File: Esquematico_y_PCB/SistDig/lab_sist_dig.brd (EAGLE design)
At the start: 93.8 x 85.2 mm, 25 parts

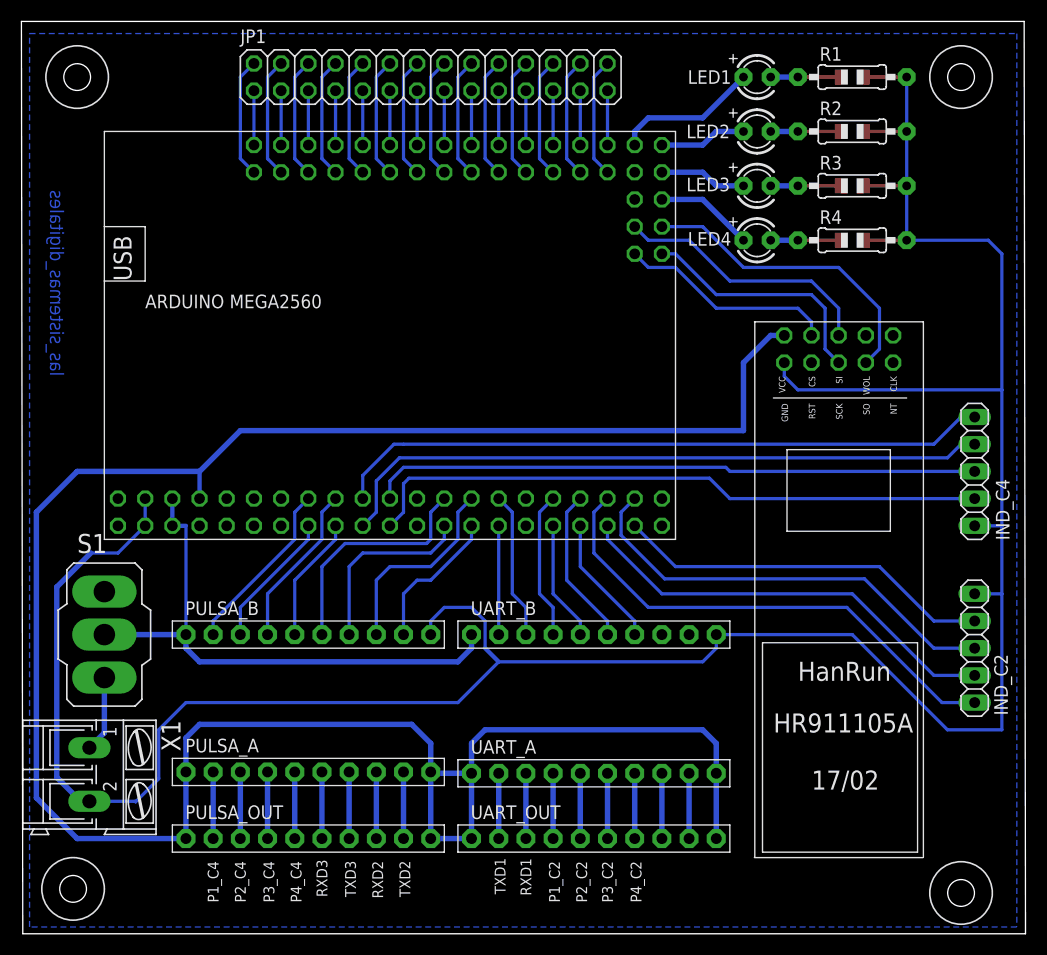
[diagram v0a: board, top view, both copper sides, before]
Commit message: PCB y Esquematico
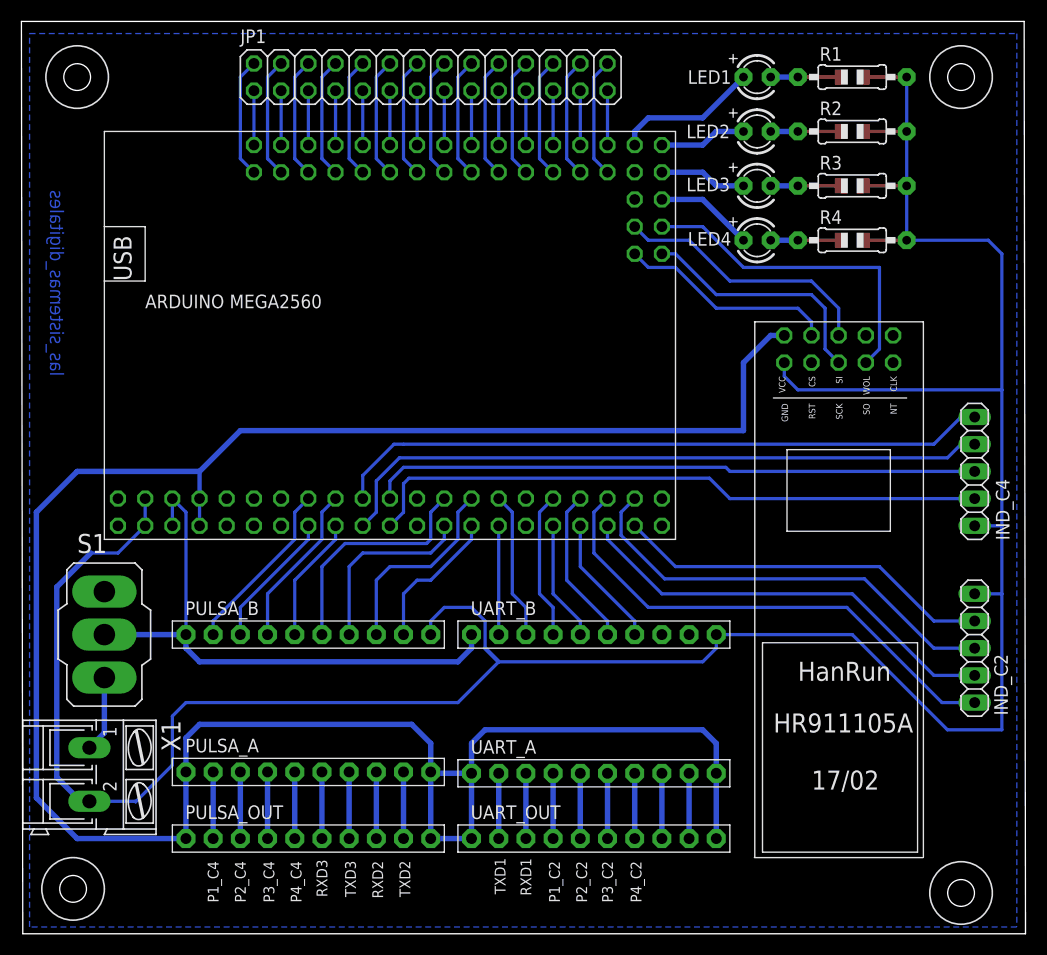
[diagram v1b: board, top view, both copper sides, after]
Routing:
- net VCC: track 216.9 -> 219.5 mm
- net SO: track 29.1 -> 31.3 mm
- net N$14: track 51.9 -> 53.6 mm
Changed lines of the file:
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@@
 <grid distance="50" unitdist="mil" unit="mm" style="lines" multiple="1" display="no" altdistance="5" altunitdist="mil" altunit="mm"/>
 <layers>
-<layer number="1" name="Top" color="4" fill="1" visible="no" active="yes"/>
+<layer number="1" name="Top" color="4" fill="1" visible="yes" active="yes"/>
 <layer number="16" name="Bottom" color="1" fill="1" visible="yes" active="yes"/>
 <layer number="17" name="Pads" color="2" fill="1" visible="yes" active="yes"/>
@@
 <layer number="19" name="Unrouted" color="6" fill="1" visible="yes" active="yes"/>
 <layer number="20" name="Dimension" color="24" fill="1" visible="yes" active="yes"/>
-<layer number="21" name="tPlace" color="7" fill="1" visible="no" active="yes"/>
-<layer number="22" name="bPlace" color="7" fill="1" visible="no" active="yes"/>
-<layer number="23" name="tOrigins" color="15" fill="1" visible="no" active="yes"/>
-<layer number="24" name="bOrigins" color="15" fill="1" visible="no" active="yes"/>
-<layer number="25" name="tNames" color="7" fill="1" visible="no" active="yes"/>
+<layer number="21" name="tPlace" color="7" fill="1" visible="yes" active="yes"/>
+<layer number="22" name="bPlace" color="7" fill="1" visible="yes" active="yes"/>
+<layer number="23" name="tOrigins" color="15" fill="1" visible="yes" active="yes"/>
+<layer number="24" name="bOrigins" color="15" fill="1" visible="yes" active="yes"/>
+<layer number="25" name="tNames" color="7" fill="1" visible="yes" active="yes"/>
 <layer number="26" name="bNames" color="7" fill="1" visible="no" active="yes"/>
 <layer number="27" name="tValues" color="7" fill="1" visible="no" active="yes"/>
@@
 <layer number="38" name="bTest" color="7" fill="1" visible="no" active="yes"/>
 <layer number="39" name="tKeepout" color="4" fill="11" visible="no" active="yes"/>
-<layer number="40" name="bKeepout" color="1" fill="11" visible="no" active="yes"/>
+<layer number="40" name="bKeepout" color="1" fill="11" visible="yes" active="yes"/>
 <layer number="41" name="tRestrict" color="4" fill="10" visible="no" active="yes"/>
-<layer number="42" name="bRestrict" color="1" fill="10" visible="no" active="yes"/>
+<layer number="42" name="bRestrict" color="1" fill="10" visible="yes" active="yes"/>
 <layer number="43" name="vRestrict" color="2" fill="10" visible="no" active="yes"/>
 <layer number="44" name="Drills" color="7" fill="1" visible="no" active="yes"/>
@@
 <contactref element="U$2" pad="SO"/>
 <wire x1="76.2" y1="54.61" x2="77.47" y2="55.88" width="0.3048" layer="16"/>
-<wire x1="60.96" y1="67.31" x2="64.77" y2="63.5" width="0.3048" layer="16"/>
+<wire x1="77.47" y1="63.5" x2="64.77" y2="63.5" width="0.3048" layer="16"/>
+<wire x1="64.77" y1="63.5" x2="60.96" y2="67.31" width="0.3048" layer="16"/>
 <wire x1="60.96" y1="67.31" x2="57.15" y2="67.31" width="0.3048" layer="16"/>
-<wire x1="77.47" y1="59.69" x2="77.47" y2="55.88" width="0.3048" layer="16"/>
-<wire x1="64.77" y1="63.5" x2="73.66" y2="63.5" width="0.3048" layer="16"/>
-<wire x1="73.66" y1="63.5" x2="77.47" y2="59.69" width="0.3048" layer="16"/>
+<wire x1="77.47" y1="55.88" x2="77.47" y2="63.5" width="0.3048" layer="16"/>
 </signal>
 <signal name="SI">
@@
 <wire x1="3.683" y1="13.6398" x2="7.9502" y2="13.6398" width="0.3048" layer="16"/>
 <wire x1="7.9502" y1="13.6398" x2="8.001" y2="13.589" width="0.3048" layer="16"/>
-<wire x1="10.16" y1="15.748" x2="10.16" y2="20.32" width="0.3048" layer="16"/>
-<wire x1="10.16" y1="20.32" x2="12.7" y2="22.86" width="0.3048" layer="16"/>
+<wire x1="11.43" y1="17.018" x2="11.43" y2="21.59" width="0.3048" layer="16"/>
+<wire x1="11.43" y1="21.59" x2="12.7" y2="22.86" width="0.3048" layer="16"/>
 <wire x1="38.1" y1="22.86" x2="41.91" y2="26.67" width="0.3048" layer="16"/>
-<wire x1="8.001" y1="13.589" x2="10.16" y2="15.748" width="0.3048" layer="16"/>
+<wire x1="8.001" y1="13.589" x2="11.43" y2="17.018" width="0.3048" layer="16"/>
 <wire x1="12.7" y1="22.86" x2="38.1" y2="22.86" width="0.3048" layer="16"/>
 <wire x1="80.01" y1="66.04" x2="80.01" y2="71.12" width="0.3048" layer="16"/>
@@
 <wire x1="3.683" y1="13.6398" x2="2.8702" y2="13.6398" width="0.508" layer="16"/>
 <wire x1="2.8702" y1="13.6398" x2="2.54" y2="13.97" width="0.508" layer="16"/>
-<wire x1="0.635" y1="15.875" x2="2.54" y2="13.97" width="0.508" layer="16"/>
+<wire x1="0.635" y1="15.875" x2="2.8702" y2="13.6398" width="0.508" layer="16"/>
 <polygon width="0.3048" layer="16" isolate="1.27">
 <vertex x="-1.905" y="1.905"/>
@@
 <contactref element="UART_A" pad="10"/>
 <contactref element="U$2" pad="VCC"/>
+<wire x1="13.97" y1="39.37" x2="13.97" y2="41.91" width="0.3048" layer="16"/>
 <wire x1="13.97" y1="20.828" x2="12.7" y2="19.558" width="0.508" layer="16"/>
 <wire x1="12.7" y1="19.558" x2="12.7" y2="16.383" width="0.508" layer="16"/>
@@
 <wire x1="-1.27" y1="40.64" x2="2.54" y2="44.45" width="0.508" layer="16"/>
 <wire x1="2.54" y1="44.45" x2="13.97" y2="44.45" width="0.508" layer="16"/>
-<wire x1="13.97" y1="41.91" x2="13.97" y2="39.37" width="0" layer="19" extent="1-1"/>
 </signal>
 <signal name="TXD1">
@@
 <contactref element="UART_B" pad="1"/>
 <contactref element="S1" pad="2"/>
-<wire x1="12.7" y1="39.37" x2="12.7" y2="29.21" width="0.3048" layer="16"/>
+<wire x1="11.43" y1="41.91" x2="12.7" y2="40.64" width="0.3048" layer="16"/>
+<wire x1="12.7" y1="40.64" x2="12.7" y2="29.21" width="0.3048" layer="16"/>
+<wire x1="11.43" y1="39.37" x2="11.43" y2="41.91" width="0.3048" layer="16"/>
 <wire x1="5.08" y1="29.21" x2="12.7" y2="29.21" width="0.508" layer="16"/>
 <wire x1="12.7" y1="29.21" x2="12.7" y2="27.94" width="0.508" layer="16"/>
@@
 <wire x1="39.37" y1="27.94" x2="39.37" y2="29.21" width="0.508" layer="16"/>
 <wire x1="13.97" y1="26.67" x2="38.1" y2="26.67" width="0.508" layer="16"/>
-<wire x1="11.43" y1="41.91" x2="11.43" y2="39.37" width="0.4064" layer="16"/>
-<wire x1="11.43" y1="39.37" x2="12.7" y2="39.37" width="0.4064" layer="16"/>
 </signal>
 <signal name="N$22">

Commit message: PCB y esquematico
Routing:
- net SO: track 31.3 -> 29.1 mm
- net GND: track 242.3 -> 241.1 mm
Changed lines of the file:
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@@
 <contactref element="U$2" pad="SO"/>
 <wire x1="76.2" y1="54.61" x2="77.47" y2="55.88" width="0.3048" layer="16"/>
-<wire x1="77.47" y1="63.5" x2="64.77" y2="63.5" width="0.3048" layer="16"/>
 <wire x1="64.77" y1="63.5" x2="60.96" y2="67.31" width="0.3048" layer="16"/>
 <wire x1="60.96" y1="67.31" x2="57.15" y2="67.31" width="0.3048" layer="16"/>
-<wire x1="77.47" y1="55.88" x2="77.47" y2="63.5" width="0.3048" layer="16"/>
+<wire x1="77.47" y1="59.69" x2="77.47" y2="55.88" width="0.3048" layer="16"/>
+<wire x1="64.77" y1="63.5" x2="73.66" y2="63.5" width="0.3048" layer="16"/>
+<wire x1="73.66" y1="63.5" x2="77.47" y2="59.69" width="0.3048" layer="16"/>
 </signal>
 <signal name="SI">
@@
 <wire x1="3.6322" y1="13.589" x2="3.683" y2="13.6398" width="0.3048" layer="16"/>
 <wire x1="0.635" y1="33.655" x2="0.635" y2="15.875" width="0.508" layer="16"/>
-<wire x1="3.683" y1="13.6398" x2="7.9502" y2="13.6398" width="0.3048" layer="16"/>
-<wire x1="7.9502" y1="13.6398" x2="8.001" y2="13.589" width="0.3048" layer="16"/>
-<wire x1="11.43" y1="17.018" x2="11.43" y2="21.59" width="0.3048" layer="16"/>
-<wire x1="11.43" y1="21.59" x2="12.7" y2="22.86" width="0.3048" layer="16"/>
+<wire x1="3.683" y1="13.6398" x2="6.7818" y2="13.6398" width="0.3048" layer="16"/>
+<wire x1="10.16" y1="17.018" x2="10.16" y2="20.32" width="0.3048" layer="16"/>
+<wire x1="10.16" y1="20.32" x2="12.7" y2="22.86" width="0.3048" layer="16"/>
 <wire x1="38.1" y1="22.86" x2="41.91" y2="26.67" width="0.3048" layer="16"/>
-<wire x1="8.001" y1="13.589" x2="11.43" y2="17.018" width="0.3048" layer="16"/>
+<wire x1="6.7818" y1="13.6398" x2="10.16" y2="17.018" width="0.3048" layer="16"/>
 <wire x1="12.7" y1="22.86" x2="38.1" y2="22.86" width="0.3048" layer="16"/>
 <wire x1="80.01" y1="66.04" x2="80.01" y2="71.12" width="0.3048" layer="16"/>
@@
 <wire x1="80.01" y1="81.28" x2="80.01" y2="76.2" width="0.3048" layer="16"/>
 <wire x1="3.683" y1="13.6398" x2="2.8702" y2="13.6398" width="0.508" layer="16"/>
-<wire x1="2.8702" y1="13.6398" x2="2.54" y2="13.97" width="0.508" layer="16"/>
 <wire x1="0.635" y1="15.875" x2="2.8702" y2="13.6398" width="0.508" layer="16"/>
 <polygon width="0.3048" layer="16" isolate="1.27">
